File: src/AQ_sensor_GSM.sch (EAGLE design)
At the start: 49 parts, among them IC2 MCP73831/OT, J1 F-1X03-SIP-100-32, SW1 PCM12SMTR, SW2 PCM12SMTR, U2 TEXAS_INSTRUMENTS_SN74HC125TE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, U3 TEXAS_INSTRUMENTS_LM1117IMP-3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, U4 ESP8266-12E/ESP-12E, U5 CH340G, X1 53048-08, X2 SIMLOCK-C707_10M006_512_2, X4 50 Ohms

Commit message: PCB Lay out Init
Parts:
- added GPS: PINHD-1X4, Connector:PINHD-1X4
- added JP1: PINHD-1X10, Connector:PINHD-1X10
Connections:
- removed net UD+: U5.UD+
- removed net UD-: U5.UD-
- new net ESP_CSO: JP1.5, U4.CS0
- new net ESP_MISO: JP1.7, U4.MISO
- new net ESP_MOSI: JP1.6, U4.MOSI
- new net ESP_SCLK: JP1.4, U4.SCLK
- new net GPS_RX: GPS.2, U4.IO9
- new net GPS_TX: GPS.3, U4.IO10
- new net IO16: JP1.8, U4.IO16
- net +5V: now also GPS.1, JP1.1
- net ADC0: now also JP1.9
- net D+: now also U5.UD+
- net D-: now also U5.UD-
- net GND: now also GPS.4, JP1.10
- net RXD: now also JP1.3
- net TXD: now also JP1.2

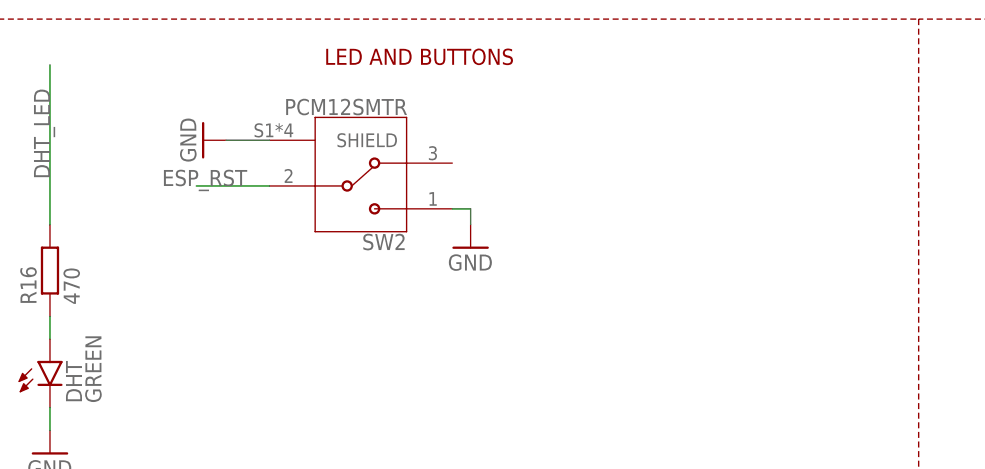
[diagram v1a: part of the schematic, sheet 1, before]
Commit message: PCB Resized
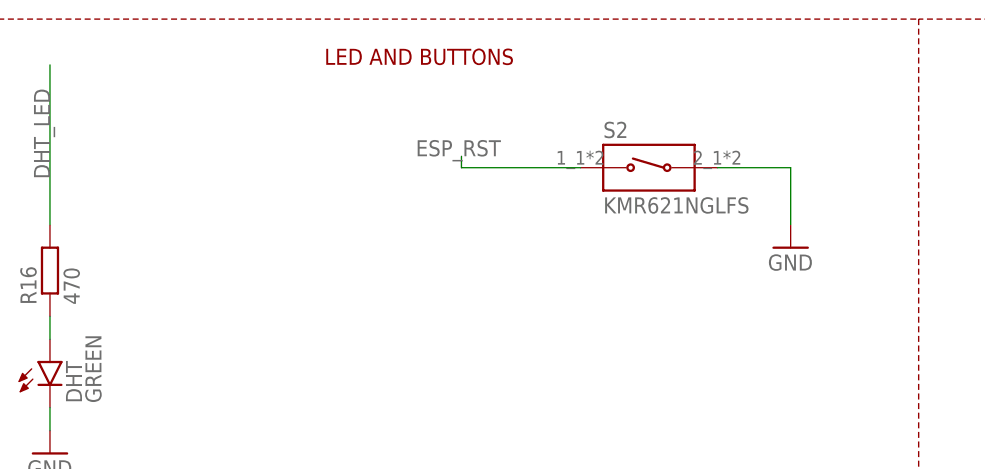
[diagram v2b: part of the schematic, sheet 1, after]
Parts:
- removed SW2: PCM12SMTR, AQ_sensor_GSM:PCM12SMTR
- added S2: KMR621NGLFS, AQ_sensor_GSM:KMR621NGLFS
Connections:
- net ESP_RST: now also S2.1; no longer SW2.2
- net GND: now also S2.2; no longer SW2.1, SW2.SHIELD
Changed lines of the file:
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@@
 <part name="GND34" library="supply1" library_urn="urn:adsk.eagle:library:371" deviceset="GND" device=""/>
 <part name="FRAME1" library="frames" library_urn="urn:adsk.eagle:library:229" deviceset="A3L-LOC" device=""/>
-<part name="GND13" library="supply1" library_urn="urn:adsk.eagle:library:371" deviceset="GND" device=""/>
 <part name="DHT" library="led" library_urn="urn:adsk.eagle:library:259" deviceset="LED" device="CHIP-LED0603" package3d_urn="urn:adsk.eagle:package:15819/3" value="GREEN"/>
 <part name="R16" library="rcl" library_urn="urn:adsk.eagle:library:334" deviceset="R-EU_" device="R0603" package3d_urn="urn:adsk.eagle:package:23555/3" value="470"/>
 <part name="GND37" library="supply1" library_urn="urn:adsk.eagle:library:371" deviceset="GND" device=""/>
 <part name="SW1" library="AQ_sensor_GSM" library_urn="urn:adsk.eagle:library:30300195" deviceset="PCM12SMTR" device="" package3d_urn="urn:adsk.eagle:package:30300294/2"/>
-<part name="SW2" library="AQ_sensor_GSM" library_urn="urn:adsk.eagle:library:30300195" deviceset="PCM12SMTR" device="" package3d_urn="urn:adsk.eagle:package:30300294/2"/>
-<part name="GND12" library="supply1" library_urn="urn:adsk.eagle:library:371" deviceset="GND" device=""/>
 <part name="FRAME2" library="frames" library_urn="urn:adsk.eagle:library:229" deviceset="A3L-LOC" device=""/>
 <part name="U1" library="AQ_sensor_GSM" library_urn="urn:adsk.eagle:library:30300195" deviceset="GSM_SIM800L" device="" package3d_urn="urn:adsk.eagle:package:30300265/2"/>
@@
 <part name="P+11" library="supply1" library_urn="urn:adsk.eagle:library:371" deviceset="+5V" device=""/>
 <part name="GND19" library="supply1" library_urn="urn:adsk.eagle:library:371" deviceset="GND" device=""/>
+<part name="S2" library="AQ_sensor_GSM" library_urn="urn:adsk.eagle:library:30300195" deviceset="KMR621NGLFS" device="" package3d_urn="urn:adsk.eagle:package:30300293/2"/>
+<part name="GND9" library="supply1" library_urn="urn:adsk.eagle:library:371" deviceset="GND" device=""/>
 </parts>
 <sheets>
@@
 <attribute name="SHEET" x="357.505" y="5.08" size="2.54" layer="94"/>
 </instance>
-<instance part="GND13" gate="1" x="136.398" y="237.998" smashed="yes" rot="R270">
-<attribute name="VALUE" x="133.858" y="240.538" size="1.778" layer="96" rot="R270"/>
-</instance>
 <instance part="DHT" gate="G$1" x="119.38" y="213.36" smashed="yes">
 <attribute name="NAME" x="122.936" y="208.788" size="1.778" layer="95" rot="R90"/>
@@
 <attribute name="VALUE" x="51.91735" y="178.825859375" size="1.778459375" layer="96" rot="R180"/>
 </instance>
-<instance part="SW2" gate="G$1" x="153.924" y="232.918" smashed="yes" rot="R180">
-<attribute name="NAME" x="159.008390625" y="227.579390625" size="1.779540625" layer="95" rot="R180"/>
-<attribute name="VALUE" x="159.10535" y="242.579859375" size="1.778459375" layer="96" rot="R180"/>
-</instance>
-<instance part="GND12" gate="1" x="166.116" y="226.06" smashed="yes">
-<attribute name="VALUE" x="163.576" y="223.52" size="1.778" layer="96"/>
-</instance>
 <instance part="GND8" gate="1" x="96.52" y="201.93" smashed="yes">
 <attribute name="VALUE" x="93.98" y="199.39" size="1.778" layer="96"/>
@@
 <instance part="GND19" gate="1" x="290.576" y="99.06" smashed="yes">
 <attribute name="VALUE" x="288.036" y="96.52" size="1.778" layer="96"/>
+</instance>
+<instance part="S2" gate="G$1" x="185.928" y="234.95" smashed="yes">
+<attribute name="NAME" x="180.848" y="238.252" size="1.778" layer="95"/>
+<attribute name="VALUE" x="180.848" y="229.87" size="1.778" layer="96"/>
+</instance>
+<instance part="GND9" gate="1" x="201.676" y="226.06" smashed="yes">
+<attribute name="VALUE" x="199.136" y="223.52" size="1.778" layer="96"/>
 </instance>
 </instances>
@@
 </segment>
 <segment>
-<pinref part="GND13" gate="1" pin="GND"/>
-<pinref part="SW2" gate="G$1" pin="SHIELD"/>
-<wire x1="138.938" y1="237.998" x2="143.764" y2="237.998" width="0.1524" layer="91"/>
-</segment>
-<segment>
-<pinref part="SW2" gate="G$1" pin="1"/>
-<pinref part="GND12" gate="1" pin="GND"/>
-<wire x1="164.084" y1="230.378" x2="166.116" y2="230.378" width="0.1524" layer="91"/>
-<wire x1="166.116" y1="230.378" x2="166.116" y2="228.6" width="0.1524" layer="91"/>
-</segment>
-<segment>
 <pinref part="PMS" gate="G$1" pin="C"/>
 <wire x1="96.52" y1="208.28" x2="96.52" y2="204.47" width="0.1524" layer="91"/>
@@
 <pinref part="GND19" gate="1" pin="GND"/>
 <wire x1="290.576" y1="101.6" x2="290.576" y2="104.14" width="0.1524" layer="91"/>
+</segment>
+<segment>
+<pinref part="GND9" gate="1" pin="GND"/>
+<pinref part="S2" gate="G$1" pin="2"/>
+<wire x1="201.676" y1="228.6" x2="201.676" y2="234.95" width="0.1524" layer="91"/>
+<wire x1="201.676" y1="234.95" x2="193.548" y2="234.95" width="0.1524" layer="91"/>
 </segment>
 </net>
@@
 <net name="ESP_RST" class="0">
 <segment>
-<pinref part="SW2" gate="G$1" pin="2"/>
-<wire x1="143.764" y1="232.918" x2="135.636" y2="232.918" width="0.1524" layer="91"/>
-<label x="131.826" y="232.918" size="1.778" layer="95"/>
-</segment>
-<segment>
 <pinref part="U4" gate="G$1" pin="RESET"/>
 <wire x1="198.12" y1="167.64" x2="180.34" y2="167.64" width="0.1524" layer="91"/>
 <label x="180.34" y="167.64" size="1.778" layer="95"/>
 </segment>
-</net>
+<segment>
+<pinref part="S2" gate="G$1" pin="1"/>
+<wire x1="178.308" y1="234.95" x2="165.1" y2="234.95" width="0.1524" layer="91"/>
+<wire x1="165.1" y1="234.95" x2="165.1" y2="236.22" width="0.1524" layer="91"/>
+<label x="160.02" y="236.22" size="1.778" layer="95"/>
+</segment>
+</net>

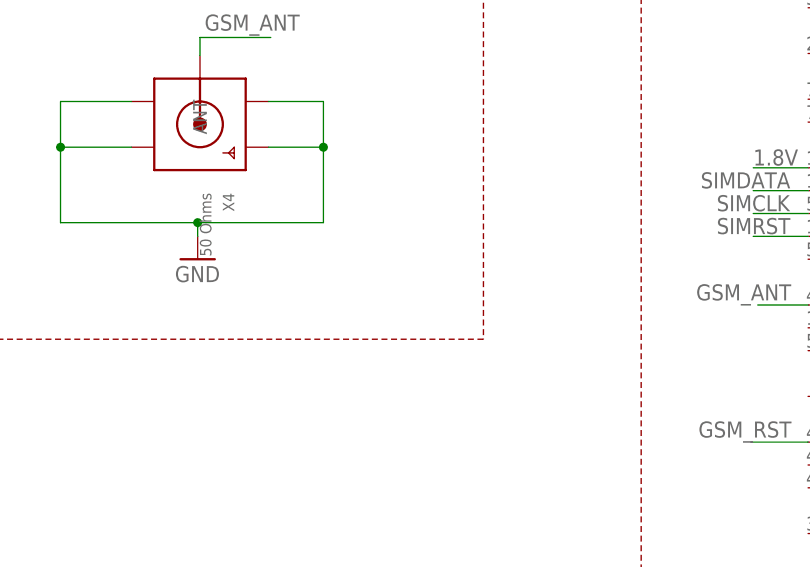
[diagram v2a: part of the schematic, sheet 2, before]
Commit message: Curved Board edges
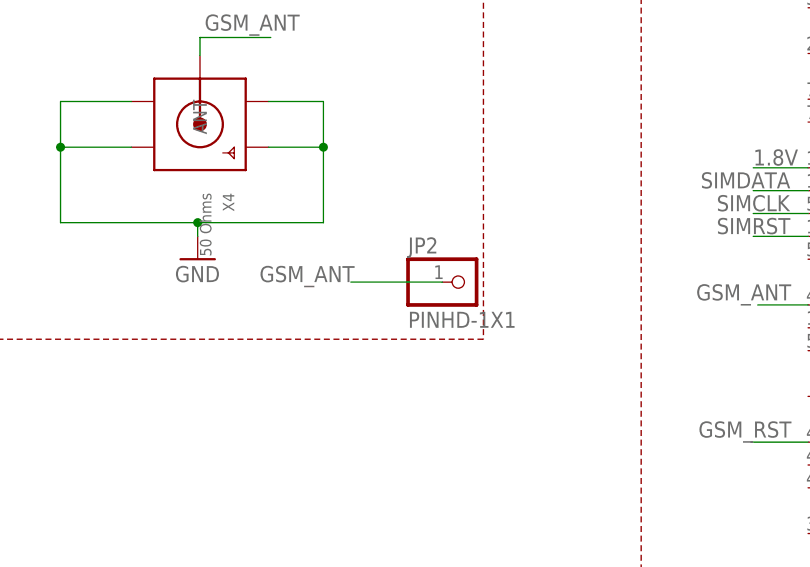
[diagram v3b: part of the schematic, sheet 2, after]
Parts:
- added JP2: PINHD-1X1, Connector:PINHD-1X1
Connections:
- net GSM_ANT: now also JP2.1
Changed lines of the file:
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@@
 <part name="S2" library="AQ_sensor_GSM" library_urn="urn:adsk.eagle:library:30300195" deviceset="KMR621NGLFS" device="" package3d_urn="urn:adsk.eagle:package:30300293/2"/>
 <part name="GND9" library="supply1" library_urn="urn:adsk.eagle:library:371" deviceset="GND" device=""/>
+<part name="JP2" library="Connector" library_urn="urn:adsk.eagle:library:16378166" deviceset="PINHD-1X1" device="" package3d_urn="urn:adsk.eagle:package:22485/2"/>
 </parts>
 <sheets>
@@
 <attribute name="VALUE" x="266.192" y="120.65" size="1.778" layer="96" rot="R180"/>
 </instance>
+<instance part="JP2" gate="G$1" x="309.88" y="76.2" smashed="yes">
+<attribute name="NAME" x="303.53" y="79.375" size="1.778" layer="95"/>
+<attribute name="VALUE" x="303.53" y="71.12" size="1.778" layer="96"/>
+</instance>
 </instances>
 <busses>
@@
 <label x="280.924" y="104.14" size="1.778" layer="95"/>
 </segment>
-</net>
+<segment>
+<pinref part="JP2" gate="G$1" pin="1"/>
+<wire x1="307.34" y1="76.2" x2="297.18" y2="76.2" width="0.1524" layer="91"/>
+<label x="287.02" y="76.2" size="1.778" layer="95"/>
+</segment>
+</net>

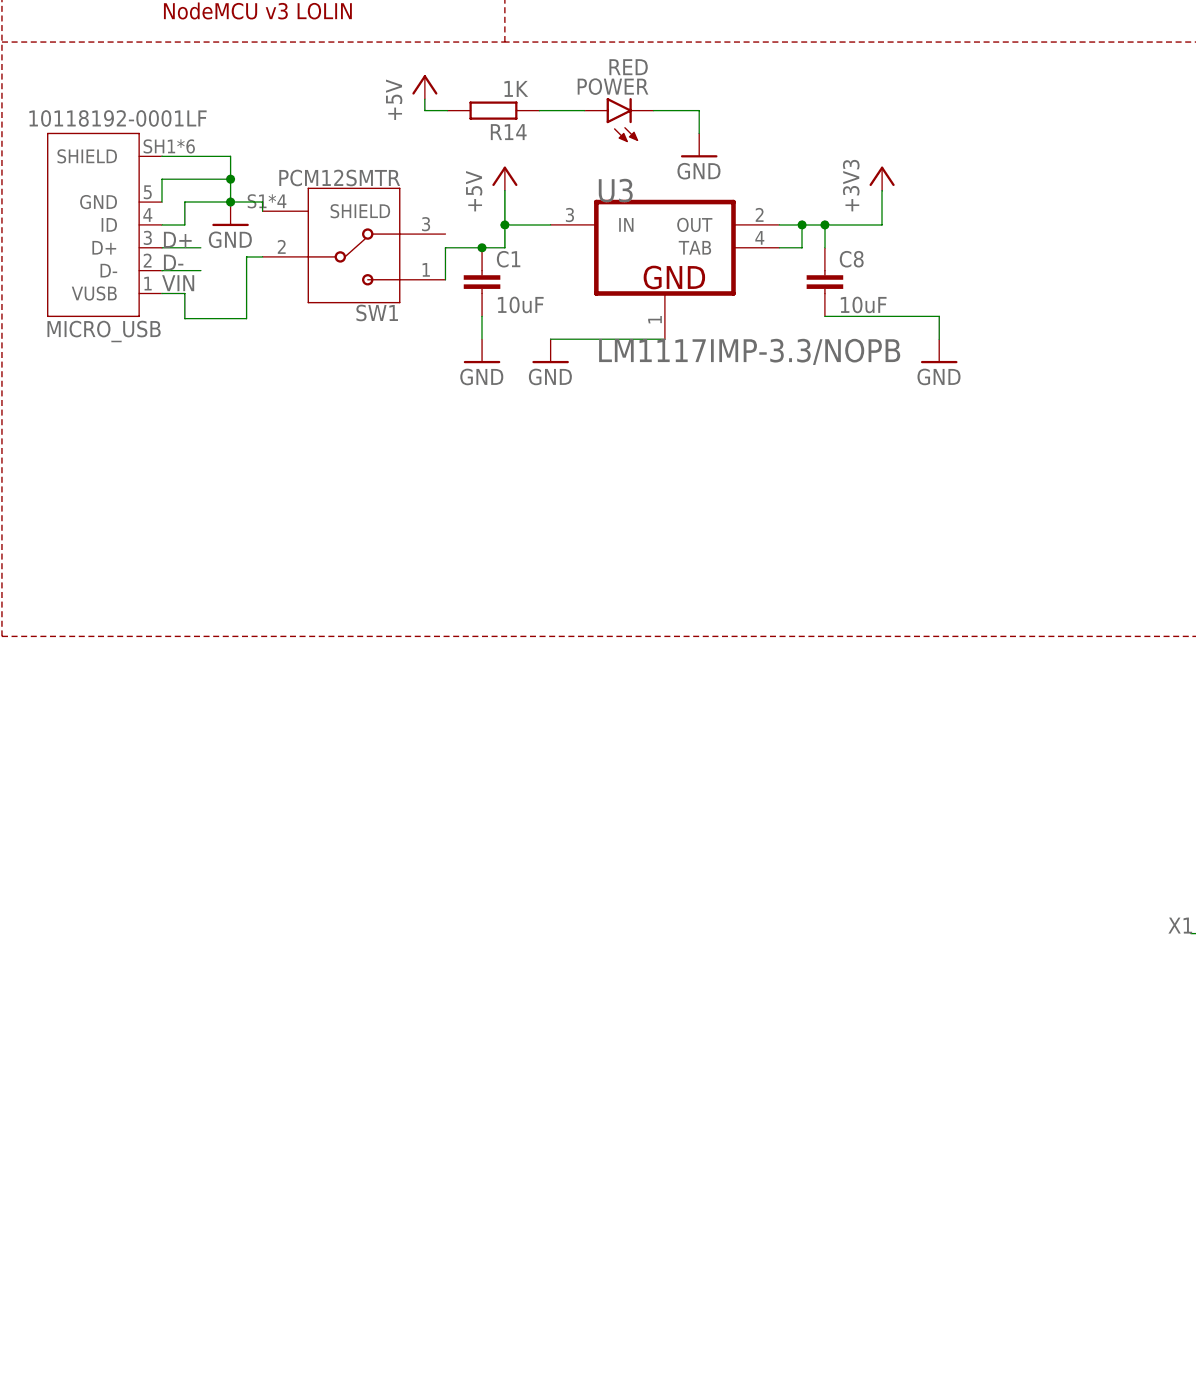
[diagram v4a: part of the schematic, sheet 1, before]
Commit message: Routed Minus Rasnet
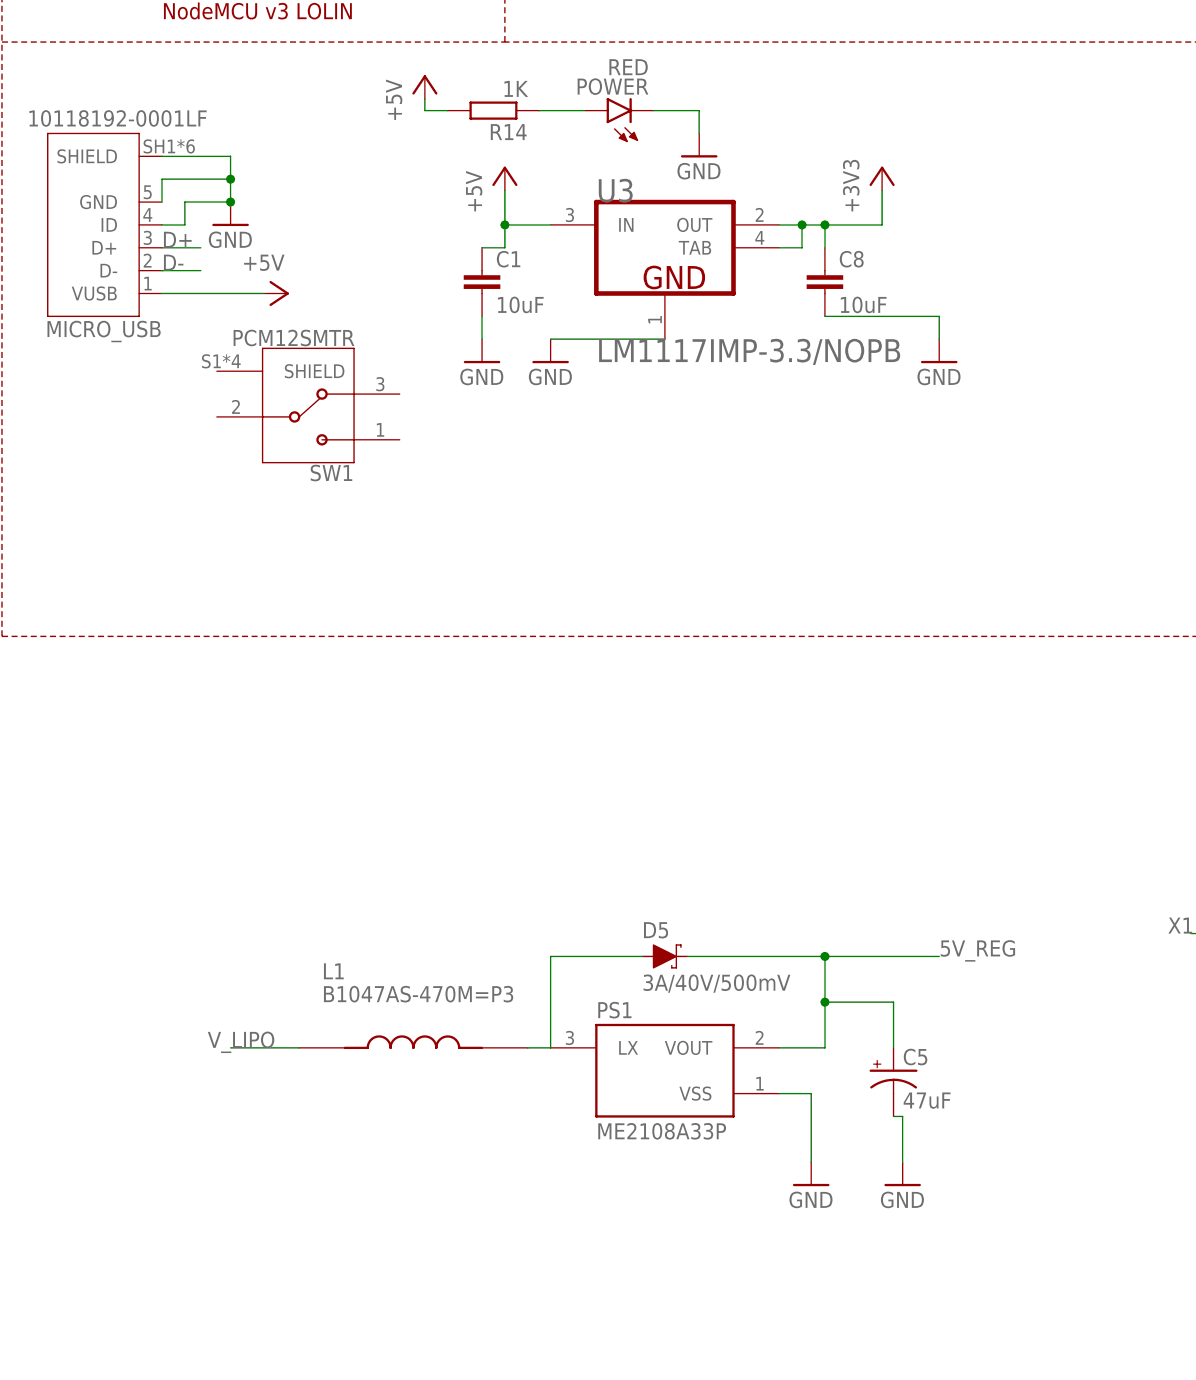
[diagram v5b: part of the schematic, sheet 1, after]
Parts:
- added C5: 47uF, SparkFun-Capacitors:47UF-POLAR-EIA3528-10V-10%
- added D5: 3A/40V/500mV, SparkFun-DiscreteSemi:DIODE-SCHOTTKY-B340A
- added L1: B1047AS-470M=P3, B1047AS-470M_P3:B1047AS-470M=P3
- added PS1: ME2108A33P, ME2108A33P:ME2108A33P
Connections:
- removed net VIN: MICRO_USB.VUSB, SW1.2
- new net 5V_REG: C5.+, D5.C, PS1.VOUT
- new net N$1: D5.A, L1.2, PS1.LX
- net +5V: now also MICRO_USB.VUSB; no longer SW1.1
- net GND: now also C5.-, PS1.VSS; no longer SW1.SHIELD
- net V_LIPO: now also L1.1
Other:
- moved on the sheet: SW1
